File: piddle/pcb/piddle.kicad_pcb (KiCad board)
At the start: 2 copper layers, 138.6 x 138 mm, 88 parts, among them J1 Conn_01x03_Socket, J10 Conn_01x03_Socket, J11 Conn_01x03_Socket, J12 Conn_01x03_Socket, J13 Conn_01x03_Socket, J14 Conn_01x03_Socket, J15 Conn_01x03_Socket, J16 infrared receiver, J17 5v, J18 3v3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

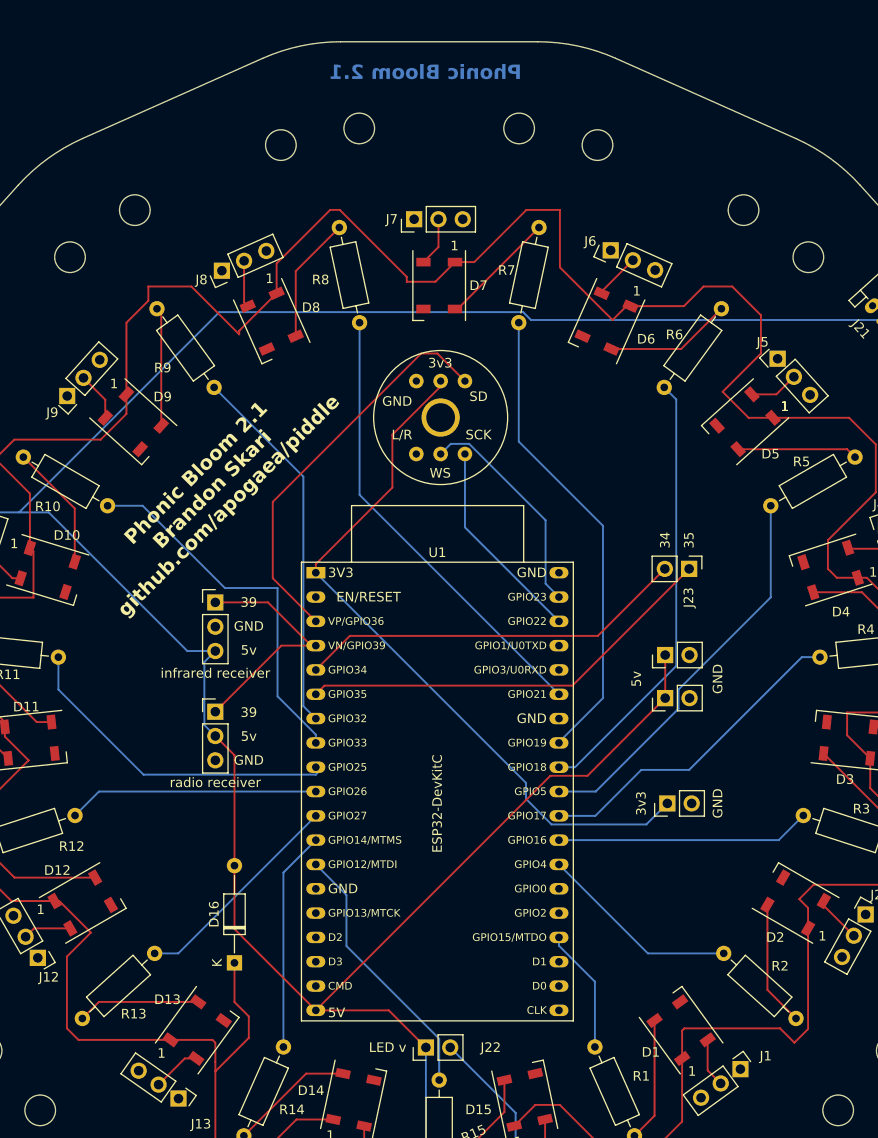
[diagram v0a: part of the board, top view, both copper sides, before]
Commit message: Avoid using GPIO 25 and 26 - they're used by DAC (and thus WiFi)
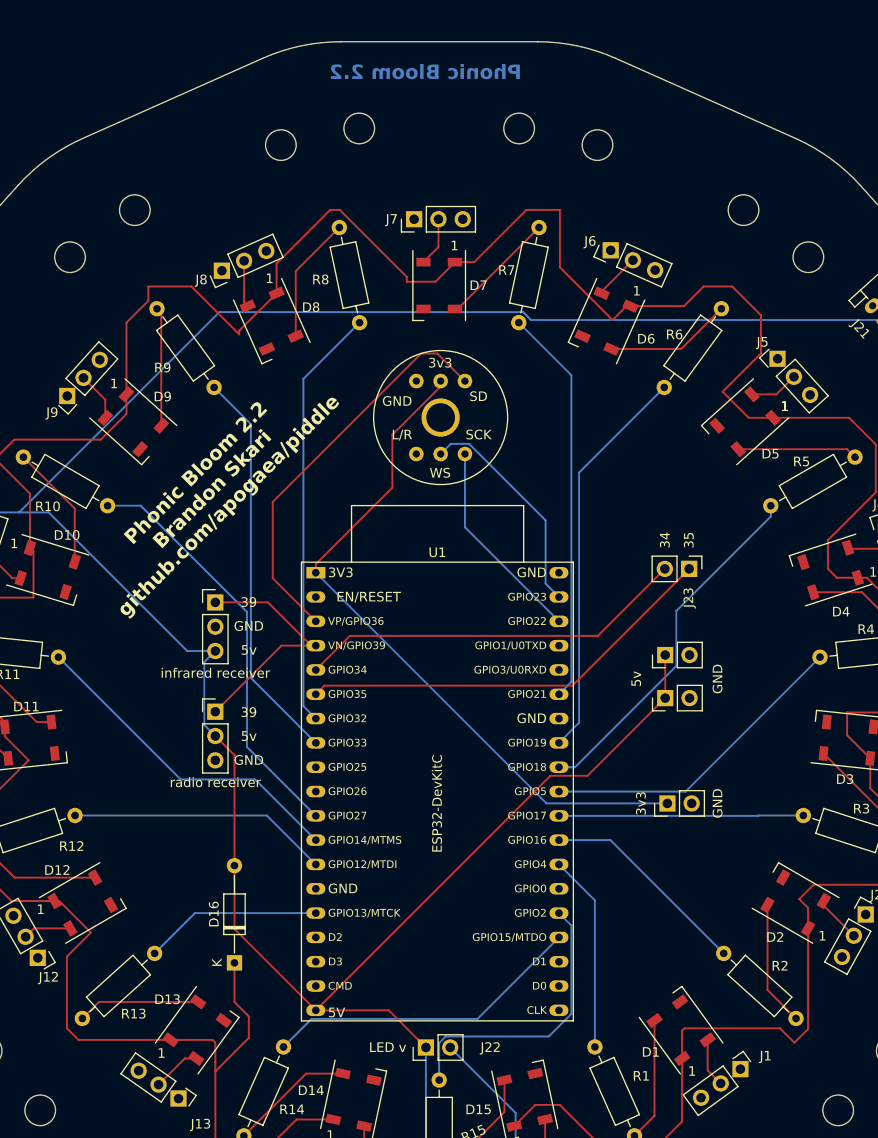
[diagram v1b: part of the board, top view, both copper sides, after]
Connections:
- R1 pad 1: /GPIO15 -> /GPIO4
- R10 pad 1: /GPIO33 -> /GPIO27
- R11 pad 1: /GPIO25 -> /GPIO14
- R12 pad 1: /GPIO26 -> /GPIO12
- R13 pad 1: /GPIO27 -> /GPIO13
- R14 pad 1: /GPIO14 -> /GPIO15
- R15 pad 1: /GPIO12 -> /GPIO2
- R2 pad 1: /GPIO4 -> /GPIO16
- R3 pad 1: /GPIO16 -> /GPIO17
- R4 pad 1: /GPIO17 -> /GPIO5
- R5 pad 1: /GPIO5 -> /GPIO18
- R6 pad 1: /GPIO18 -> /GPIO19
- R7 pad 1: /GPIO19 -> /GPIO21
- R8 pad 1: /GPIO21 -> /GPIO32
- R9 pad 1: /GPIO32 -> /GPIO33
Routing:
- net /GPIO25: track 35.3 -> 0.00 mm
- net /GPIO2: track 0.00 -> 30.0 mm
- net /GPIO26: track 26.2 -> 0.00 mm
- net /GPIO27: track 22.8 -> 43.4 mm
- net /GPIO15: track 13.0 -> 33.5 mm
- net /GPIO13: track 0.00 -> 18.6 mm
- net /GPIO14: track 23.0 -> 34.8 mm
- net /GPIO18: track 46.3 -> 37.5 mm
- net /GPIO17: track 34.1 -> 25.5 mm
- net /GPIO5: track 41.3 -> 33.1 mm
- net /GPIO19: track 49.5 -> 41.7 mm
- net /GPIO21: track 47.5 -> 41.6 mm
- net /GPIO32: track 39.0 -> 44.3 mm
- net /GPIO16: track 26.6 -> 22.1 mm
- net +3.3V: track 74.9 -> 72.1 mm
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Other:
- board text added: "Phonic Bloom 2.2"
- board text added: "Phonic Bloom 2.2 Brandon Skari github.com/apogaea/piddle"
- board text removed: "Phonic Bloom 2.1"
- board text removed: "Phonic Bloom 2.1 Brandon Skari github.com/apogaea/piddle"

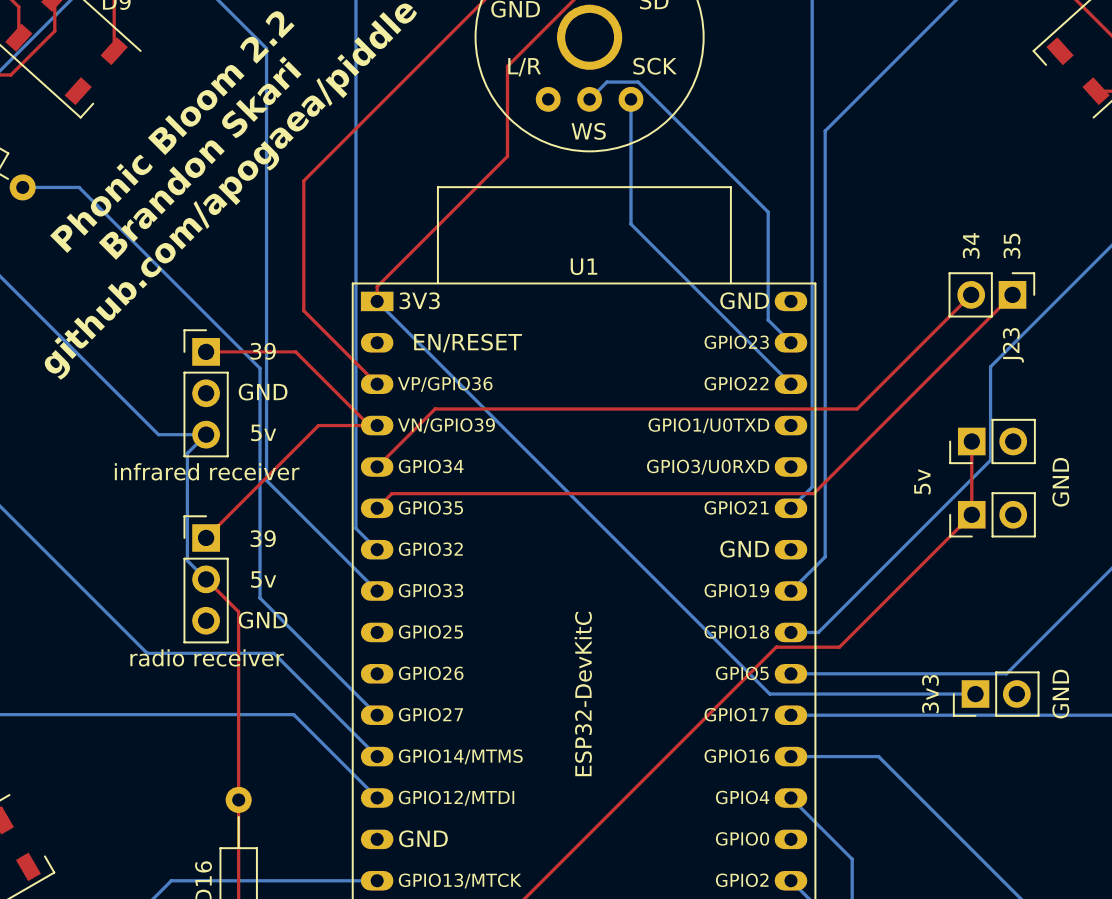
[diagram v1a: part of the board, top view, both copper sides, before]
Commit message: Move pins around for RF radio module
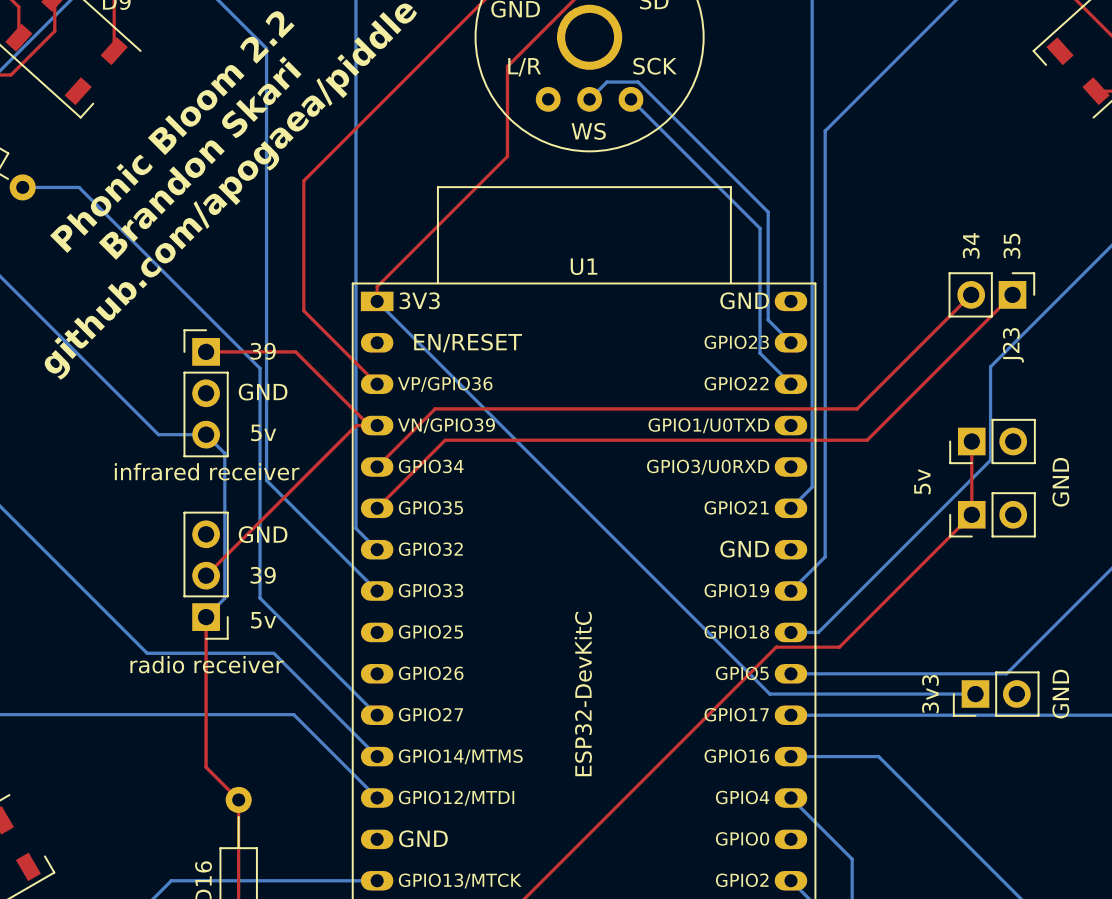
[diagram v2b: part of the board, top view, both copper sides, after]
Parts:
- moved J24 4.85 mm to (76.6, 106.4), turned to 180 degrees
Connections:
- J24 pad 1: /GPIO39 -> +5V
- J24 pad 2: +5V -> /GPIO39
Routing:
- net /GPIO39: track 25.7 -> 26.7 mm
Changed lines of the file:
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@@
 	(footprint "Connector_PinHeader_2.54mm:PinHeader_1x03_P2.54mm_Vertical"
 		(layer "F.Cu")
-		(at 76.61328 101.516343)
+		(at 76.61328 106.371343 180)
 		(descr "Through hole straight pin header, 1x03, 2.54mm pitch, single row")
 		(tags "Through hole pin header THT 1x03 2.54mm single row")
@@
 		)
 		(property "Value" "radio receiver"
-			(at 0 7.41 0)
+			(at 0 -2.975 0)
 			(layer "F.SilkS")
 			(effects
@@
 		(attr through_hole)
 		(fp_line
-			(start -1.33 -1.33)
-			(end 0 -1.33)
+			(start 1.33 1.27)
+			(end 1.33 6.41)
 			(stroke
 				(width 0.12)
@@
 		)
 		(fp_line
-			(start -1.33 0)
-			(end -1.33 -1.33)
+			(start -1.33 6.41)
+			(end 1.33 6.41)
 			(stroke
 				(width 0.12)
@@
 		(fp_line
 			(start -1.33 1.27)
-			(end -1.33 6.41)
+			(end 1.33 1.27)
 			(stroke
 				(width 0.12)
@@
 		(fp_line
 			(start -1.33 1.27)
-			(end 1.33 1.27)
+			(end -1.33 6.41)
 			(stroke
 				(width 0.12)
@@
 		)
 		(fp_line
-			(start -1.33 6.41)
-			(end 1.33 6.41)
+			(start -1.33 0)
+			(end -1.33 -1.33)
 			(stroke
 				(width 0.12)
@@
 		)
 		(fp_line
-			(start 1.33 1.27)
-			(end 1.33 6.41)
+			(start -1.33 -1.33)
+			(end 0 -1.33)
 			(stroke
 				(width 0.12)
@@
 		)
 		(fp_line
-			(start -1.8 -1.8)
-			(end -1.8 6.85)
+			(start 1.8 6.85)
+			(end 1.8 -1.8)
 			(stroke
 				(width 0.05)
@@
 		)
 		(fp_line
-			(start -1.8 6.85)
-			(end 1.8 6.85)
+			(start 1.8 -1.8)
+			(end -1.8 -1.8)
 			(stroke
 				(width 0.05)
@@
 		)
 		(fp_line
-			(start 1.8 -1.8)
-			(end -1.8 -1.8)
+			(start -1.8 6.85)
+			(end 1.8 6.85)
 			(stroke
 				(width 0.05)
@@
 		)
 		(fp_line
-			(start 1.8 6.85)
-			(end 1.8 -1.8)
+			(start -1.8 -1.8)
+			(end -1.8 6.85)
 			(stroke
 				(width 0.05)
@@
 		)
 		(fp_line
-			(start -1.27 -0.635)
-			(end -0.635 -1.27)
+			(start 1.27 6.35)
+			(end -1.27 6.35)
 			(stroke
 				(width 0.1)
@@
 		)
 		(fp_line
-			(start -1.27 6.35)
-			(end -1.27 -0.635)
+			(start 1.27 -1.27)
+			(end 1.27 6.35)
 			(stroke
 				(width 0.1)
@@
 		)
 		(fp_line
-			(start 1.27 -1.27)
-			(end 1.27 6.35)
+			(start -1.27 6.35)
+			(end -1.27 -0.635)
 			(stroke
 				(width 0.1)
@@
 		)
 		(fp_line
-			(start 1.27 6.35)
-			(end -1.27 6.35)
+			(start -1.27 -0.635)
+			(end -0.635 -1.27)
 			(stroke
 				(width 0.1)
@@
 		)
 		(pad "1" thru_hole rect
-			(at 0 0)
+			(at 0 0 180)
 			(size 1.7 1.7)
 			(drill 1)
 			(layers "*.Cu" "*.Mask")
 			(remove_unused_layers no)
-			(net 4 "/GPIO39")
+			(net 12 "+5V")
 			(pinfunction "Pin_1")
 			(pintype "passive")
 		)
 		(pad "2" thru_hole oval
-			(at 0 2.54)
+			(at 0 2.54 180)
 			(size 1.7 1.7)
 			(drill 1)
 			(layers "*.Cu" "*.Mask")
 			(remove_unused_layers no)
-			(net 12 "+5V")
+			(net 4 "/GPIO39")
 			(pinfunction "Pin_2")
 			(pintype "passive")
 		)
 		(pad "3" thru_hole oval
-			(at 0 5.08)
+			(at 0 5.08 180)
 			(size 1.7 1.7)
 			(drill 1)
@@
 	)
 	(gr_text "39"
-		(at 80.11328 101.596343 0)
+		(at 80.11328 103.846343 0)
 		(layer "F.SilkS")
 		(effects
@@
 	)
 	(gr_text "5v"
-		(at 80.11328 104.096343 0)
+		(at 80.11328 106.596343 0)
 		(layer "F.SilkS")
 		(effects
@@
 	)
 	(gr_text "GND"
-		(at 80.11328 106.596343 0)
+		(at 80.11328 101.346343 0)
 		(layer "F.SilkS")
 		(effects
@@
 	)
 	(segment
-		(start 83.51328 94.616343)
-		(end 76.61328 101.516343)
+		(start 87.11328 94.616343)
+		(end 85.82828 94.616343)
 		(width 0.2)
 		(layer "F.Cu")
@@
 	(segment
 		(start 87.11328 94.616343)
-		(end 83.51328 94.616343)
+		(end 86.63328 94.616343)
 		(width 0.2)
 		(layer "F.Cu")
@@
 	)
 	(segment
-		(start 87.11328 94.616343)
-		(end 86.63328 94.616343)
+		(start 85.82828 94.616343)
+		(end 76.61328 103.831343)
 		(width 0.2)
 		(layer "F.Cu")
@@
 	)
 	(segment
-		(start 113.91328 98.796343)
-		(end 88.01328 98.796343)
+		(start 91.29228 95.517343)
+		(end 87.11328 99.696343)
 		(width 0.2)
 		(layer "F.Cu")
@@
 	)
 	(segment
-		(start 88.01328 98.796343)
-		(end 87.11328 99.696343)
+		(start 117.19228 95.517343)
+		(end 91.29228 95.517343)
 		(width 0.2)
 		(layer "F.Cu")
@@
 	(segment
 		(start 126.11328 86.596343)
-		(end 113.91328 98.796343)
+		(end 117.19228 95.517343)
 		(width 0.2)
 		(layer "F.Cu")
@@
 	)
 	(segment
-		(start 78.61328 117.596343)
-		(end 78.61328 106.056343)
-		(width 0.2)
-		(layer "F.Cu")
-		(net 12)
-	)
-	(segment
 		(start 87.11328 132.716343)
 		(end 94.73328 132.716343)
@@
 	)
 	(segment
-		(start 78.61328 106.056343)
-		(end 76.61328 104.056343)
-		(width 0.2)
-		(layer "F.Cu")
-		(net 12)
-	)
-	(segment
 		(start 94.73328 132.716343)
 		(end 98.61328 136.596343)
@@
 	)
 	(segment
+		(start 76.61328 106.371343)
+		(end 76.61328 115.596343)
+		(width 0.2)
+		(layer "F.Cu")
+		(net 12)
+	)
+	(segment
+		(start 76.61328 115.596343)
+		(end 78.61328 117.596343)
+		(width 0.2)
+		(layer "F.Cu")
+		(net 12)
+	)
+	(segment
 		(start 146.61328 60.596343)
 		(end 109.594378 60.596343)
@@
 	)
 	(segment
-		(start 108.772135 59.7741)
-		(end 77.03341 59.7741)
+		(start 77.76428 96.327343)
+		(end 77.76428 105.220343)
 		(width 0.2)
 		(layer "B.Cu")
@@
 	)
 	(segment
-		(start 75.46228 102.905343)
-		(end 76.61328 104.056343)
+		(start 108.772135 59.7741)
+		(end 77.03341 59.7741)
 		(width 0.2)
 		(layer "B.Cu")
@@
 	)
 	(segment
-		(start 75.46228 96.327343)
-		(end 75.46228 102.905343)
+		(start 76.61328 95.176343)
+		(end 77.76428 96.327343)
 		(width 0.2)
 		(layer "B.Cu")
@@
 	)
 	(segment
-		(start 76.61328 95.176343)
-		(end 75.46228 96.327343)
+		(start 77.76428 105.220343)
+		(end 76.61328 106.371343)
 		(width 0.2)
 		(layer "B.Cu")
@@
 	)
 	(segment
+		(start 110.61328 82.516343)
+		(end 110.61328 90.176343)
+		(width 0.2)
+		(layer "B.Cu")
+		(net 30)
+	)
+	(segment
 		(start 102.69328 74.596343)
-		(end 102.69328 82.256343)
+		(end 110.61328 82.516343)
 		(width 0.2)
 		(layer "B.Cu")
@@
 	)
 	(segment
-		(start 102.69328 82.256343)
+		(start 110.61328 90.176343)
 		(end 112.51328 92.076343)
 		(width 0.2)

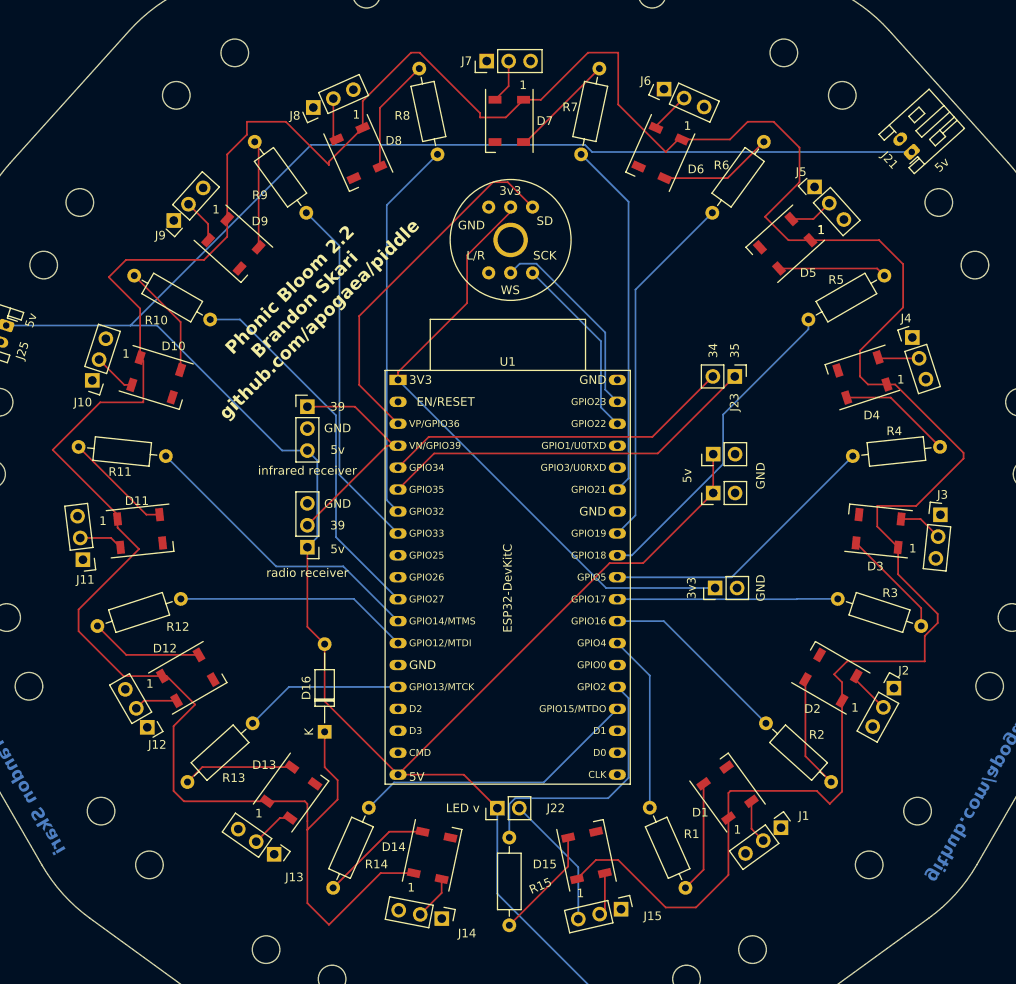
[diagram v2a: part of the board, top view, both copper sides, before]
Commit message: Don't use pins used by WiFi
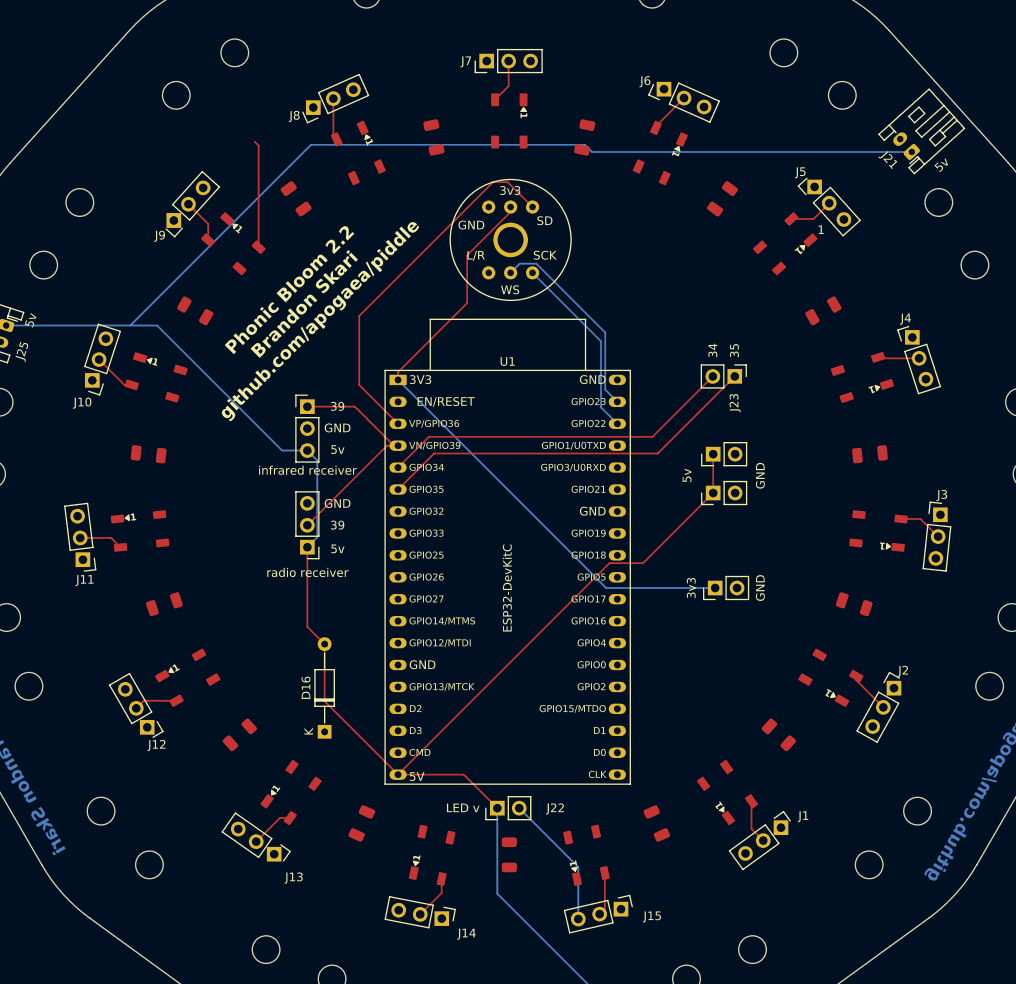
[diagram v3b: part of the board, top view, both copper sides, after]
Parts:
- D1, D10, D11, D12, D13, D14, D15, D2, D3, D4, D5, D6, D7, D8, D9: footprint LED_SMD:LED_WS2812B_PLCC4_5.0x5.0mm_P3.2mm -> PCM_JLCPCB:LED_WS2812B_PLCC4_5.0x5.0mm_P3.2mm
- R1, R10, R11, R12, R13, R14, R15, R2, R3, R4, R5, R6, R7, R8, R9: footprint Resistor_THT:R_Axial_DIN0207_L6.3mm_D2.5mm_P10.16mm_Horizontal -> PCM_JLCPCB:R_1206
- moved R5 2.00 mm to (136.4, 79.0)
- moved R10 2.00 mm to (63.6, 79.0)
- moved R13 2.00 mm to (68.8, 128.1)
- moved R2 2.00 mm to (131.2, 128.1)
- moved R15 2.00 mm to (100.0, 142.0)
- moved R7 2.00 mm to (108.7, 58.9)
- moved R8 2.00 mm to (91.3, 58.9)
- moved R6 2.00 mm to (124.7, 66.0)
- moved R9 2.00 mm to (75.3, 66.0)
- moved R1 2.00 mm to (117.1, 138.4)
- moved R14 2.00 mm to (82.9, 138.4)
- moved R12 2.00 mm to (60.1, 113.0)
- moved R3 2.00 mm to (139.9, 113.0)
- moved R4 2.00 mm to (141.8, 95.6)
- moved R11 2.00 mm to (58.2, 95.6)
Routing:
- net /4.3V: track 427.3 -> 0.00 mm
- net /GPIO32: track 44.3 -> 0.00 mm
- net /GPIO27: track 43.4 -> 0.00 mm
- net /GPIO19: track 41.7 -> 0.00 mm
- net /GPIO21: track 41.6 -> 0.00 mm
- net /GPIO33: track 41.5 -> 0.00 mm
- net /GPIO18: track 37.5 -> 0.00 mm
- net /GPIO14: track 34.8 -> 0.00 mm
- net /GPIO15: track 33.5 -> 0.00 mm
- net /GPIO5: track 33.1 -> 0.00 mm
- net /GPIO2: track 30.0 -> 0.00 mm
- net /GPIO12: track 27.3 -> 0.00 mm
- net /GPIO17: track 25.5 -> 0.00 mm
- net /GPIO16: track 22.1 -> 0.00 mm
- net /GPIO4: track 20.6 -> 0.00 mm
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
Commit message: Add 433 MHz radio receiver pins
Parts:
- removed J24: radio receiver, Connector_PinHeader_2.54mm:PinHeader_1x03_P2.54mm_Vertical
- added radio receiver: 433 MHz receiver, Connector_PinHeader_2.54mm:PinHeader_1x04_P2.54mm_Vertical, F.Cu at (76.6, 101.5)
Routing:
- net /4.3V: track 0.00 -> 289.3 mm
- net /GPIO21: track 0.00 -> 54.9 mm
- net /GPIO32: track 0.00 -> 54.3 mm
- net /GPIO19: track 0.00 -> 45.4 mm
- net /GPIO33: track 0.00 -> 43.5 mm
- net /GPIO27: track 0.00 -> 41.9 mm
- net /GPIO18: track 0.00 -> 41.7 mm
- net /GPIO15: track 0.00 -> 40.3 mm
- net /GPIO14: track 0.00 -> 35.4 mm
- net /GPIO5: track 0.00 -> 33.6 mm
- net /GPIO12: track 0.00 -> 27.7 mm
- net /GPIO17: track 0.00 -> 26.1 mm
- net /GPIO13: track 0.00 -> 25.5 mm
- net /GPIO2: track 0.00 -> 23.2 mm
- net /GPIO16: track 0.00 -> 22.7 mm
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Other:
- board text removed: "${REFERENCE}"
